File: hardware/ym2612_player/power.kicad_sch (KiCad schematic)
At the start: 15 parts, among them U1 LP5907MFX-4.5

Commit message: Apply the Rev A fix register: decoupling, single ground, A.VCC filter, TPA6132A2
Schematic
- YM2612 A.VCC (pin 22) gets its own 10 ohm + 220 uF + 100 nF filter.
- /IC, A0, A1 pull-downs 10k -> 4.7k (RP2350 erratum E9).
- Headphone amp: NJM4556A replaced by a TPA6132A2 at -6 dB, no output caps,
  enabled by GP12 (HP_EN, 4.7k pull-down) so power-up doesn't pop.
- 47 uF electrolytic damps the L1/C4 resonance before the LP5907.
- GNDA merged into GND; NT1 removed. Four M3 holes for the LCD standoffs.
- Ferrite label 220R@100MHz to match BLM18PG221SN1D; C15/C22 spec X7R 50V;
  LED lead note for PCBWay.
- Pico Plus 2 and its headers marked do-not-fit (Joey supplies them);
  sockets are Sullins PPTC201LFBN-RC.

Layout
- Decoupling caps placed at the pin they serve (design.NEAR), 2-7 mm instead
  of 16-70 mm.
- One solid GND plane on both layers plus 332 stitching vias (tools/stitch.py).
- J6 moved out from under the LCD backpack; encoder moved below the LCD so
  the knob clears it.
- Re-routed with Freerouting; KiCad 7 DRC: 0 errors, 0 unconnected.

Co-Authored-By: Claude Opus 5.5 (1M context) <noreply@anthropic.com>
Claude-Session: https://claude.ai/code/session_01T6y8roX1LzS9uTuKVQBe9X
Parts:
- removed NT1: GND-GNDA join, NetTie:NetTie-2_SMD_Pad2.0mm, symbol Device:NetTie_2
- added C7: 47uF, Capacitor_SMD:CP_Elec_5x5.4, symbol Device:C_Polarized
- added H1: M3, MountingHole:MountingHole_3.2mm_M3, symbol Mechanical:MountingHole
- added H6, H7, H8: M3 (LCD), MountingHole:MountingHole_3.2mm_M3, symbol Mechanical:MountingHole
- C5: renamed from U1; value LP5907MFX-4.5 -> 47uF; footprint Package_TO_SOT_SMD:SOT-23-5 -> Capacitor_SMD:CP_Elec_5x5.4; symbol Regulator_Linear:LP5907MFX-4.5 -> Device:C_Polarized; MPN LP5907MFX-4.5/NOPB -> (none); Spec low-noise LDO, 4.5V, 250mA -> electrolytic, 16V
- C6: value 47uF -> 4.7uF; footprint Capacitor_SMD:CP_Elec_5x5.4 -> Capacitor_SMD:C_0805_2012Metric; symbol Device:C_Polarized -> Device:C; Spec electrolytic, 16V -> X5R, 10V, 0805
- FB1, FB2: value 600R@100MHz -> 220R@100MHz
- H5: renamed from H4; value M3 -> M3 (LCD)
- U1: renamed from C5; value 4.7uF -> LP5907MFX-4.5; footprint Capacitor_SMD:C_0805_2012Metric -> Package_TO_SOT_SMD:SOT-23-5; symbol Device:C -> Regulator_Linear:LP5907MFX-4.5; MPN (none) -> LP5907MFX-4.5/NOPB; Spec X5R, 10V, 0805 -> low-noise LDO, 4.5V, 250mA
- renumbered H1 to H2, H2 to H3, H3 to H4
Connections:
- net GNDA is gone; now on net GND: C5.2, C6.2, U1.2 (GND)
- net +4V5A: now also U1.5 (OUT), C7.1; no longer C5.5 (OUT), U1.1
- net GND: now also C7.2
- net VA_IN: now also U1.1 (IN), U1.3 (EN); no longer C5.3 (EN)
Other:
- note added: "Mounting holes: M3, positions set by the enclosure. H5-H8 hold the LCD module's standoffs."
- note added: "POWER: everything runs from the Pico Plus 2's own USB-C port (VBUS, 5V, up to 500 mA from a computer). +5V = VBUS from the Pico (pin 40). Feeds the LCD, backlight, window LEDs. +5V_YM = +5V through a ferrite: YM2612 and the two 74HCT541 buffers. +4V5A = quiet analog rail: ferrite + 10uH/22uF+47uF filter + LP5907 4.5V low-noise LDO. Op-amps and headphone amp. +3V3 = made by the regulator on the Pi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"
- note removed: "Mounting holes: M3, positions set by the enclosure."
- note removed: "POWER: everything runs from the Pico Plus 2's own USB-C port (VBUS, 5V, up to 500 mA from a computer). +5V = VBUS from the Pico (pin 40). Feeds the LCD, backlight, window LEDs. +5V_YM = +5V through a ferrite: YM2612 and the two 74HCT541 buffers. +4V5A = quiet analog rail: ferrite + 10uH/22uF filter + LP5907 4.5V low-noise LDO. Op-amps only. +3V3 = made by the regulator on the Pico board. GND (dig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"
- moved on the sheet: H2, H3, H4, H5

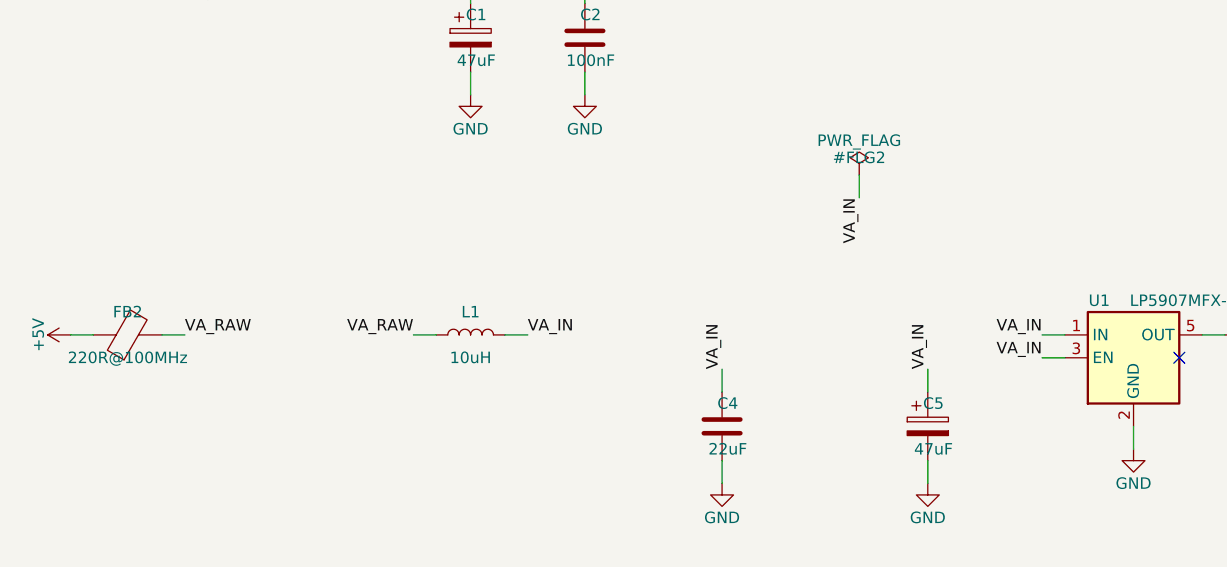
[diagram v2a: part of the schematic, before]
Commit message: Schematic: draw real wires between parts instead of name tags
tools/wires.py routes each page's nets on the 1.27 mm grid around part bodies and text.
Power pins keep power symbols (neighbouring pins share one), signals that leave a page get
one global label, and the netlist check still matches design.py exactly (0 mismatches).
Sound chip and audio pages re-laid out so the wiring reads left to right; title blocks say Rev B.

Co-Authored-By: Claude Opus 5.5 <noreply@anthropic.com>
Claude-Session: https://claude.ai/code/session_01TDTDVidYRoyJdUGgsyVTSw
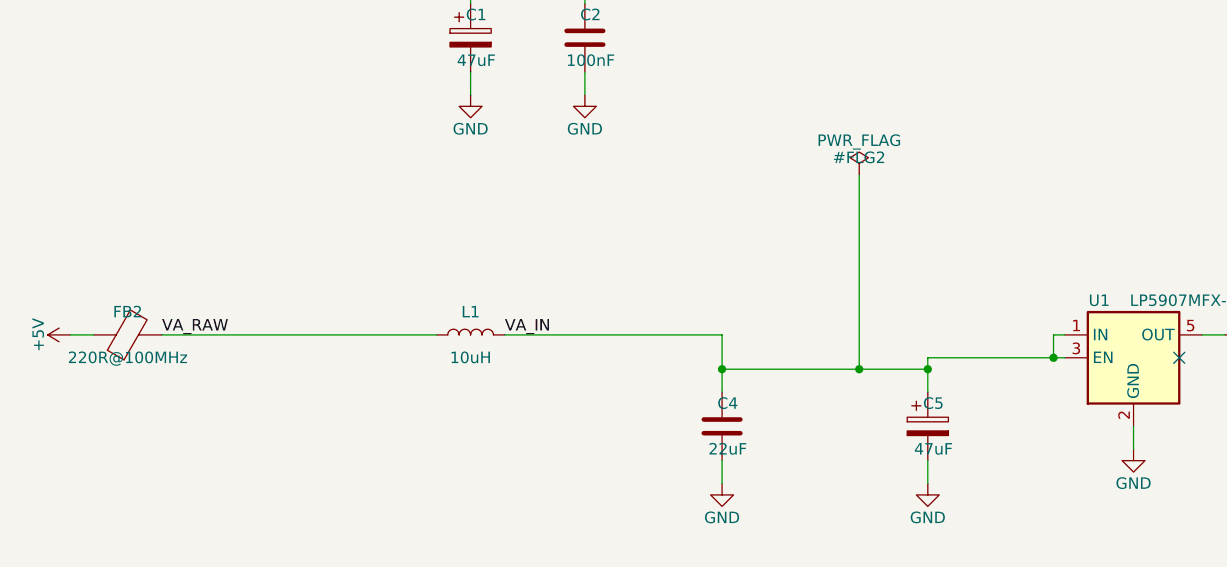
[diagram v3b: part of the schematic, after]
